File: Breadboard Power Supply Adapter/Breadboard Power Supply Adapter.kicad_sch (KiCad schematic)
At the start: 17 parts, among them J1 Conn_02x03_Odd_Even, J2 Conn_02x03_Odd_Even, J3 Conn_01x02, J4 Conn_01x02

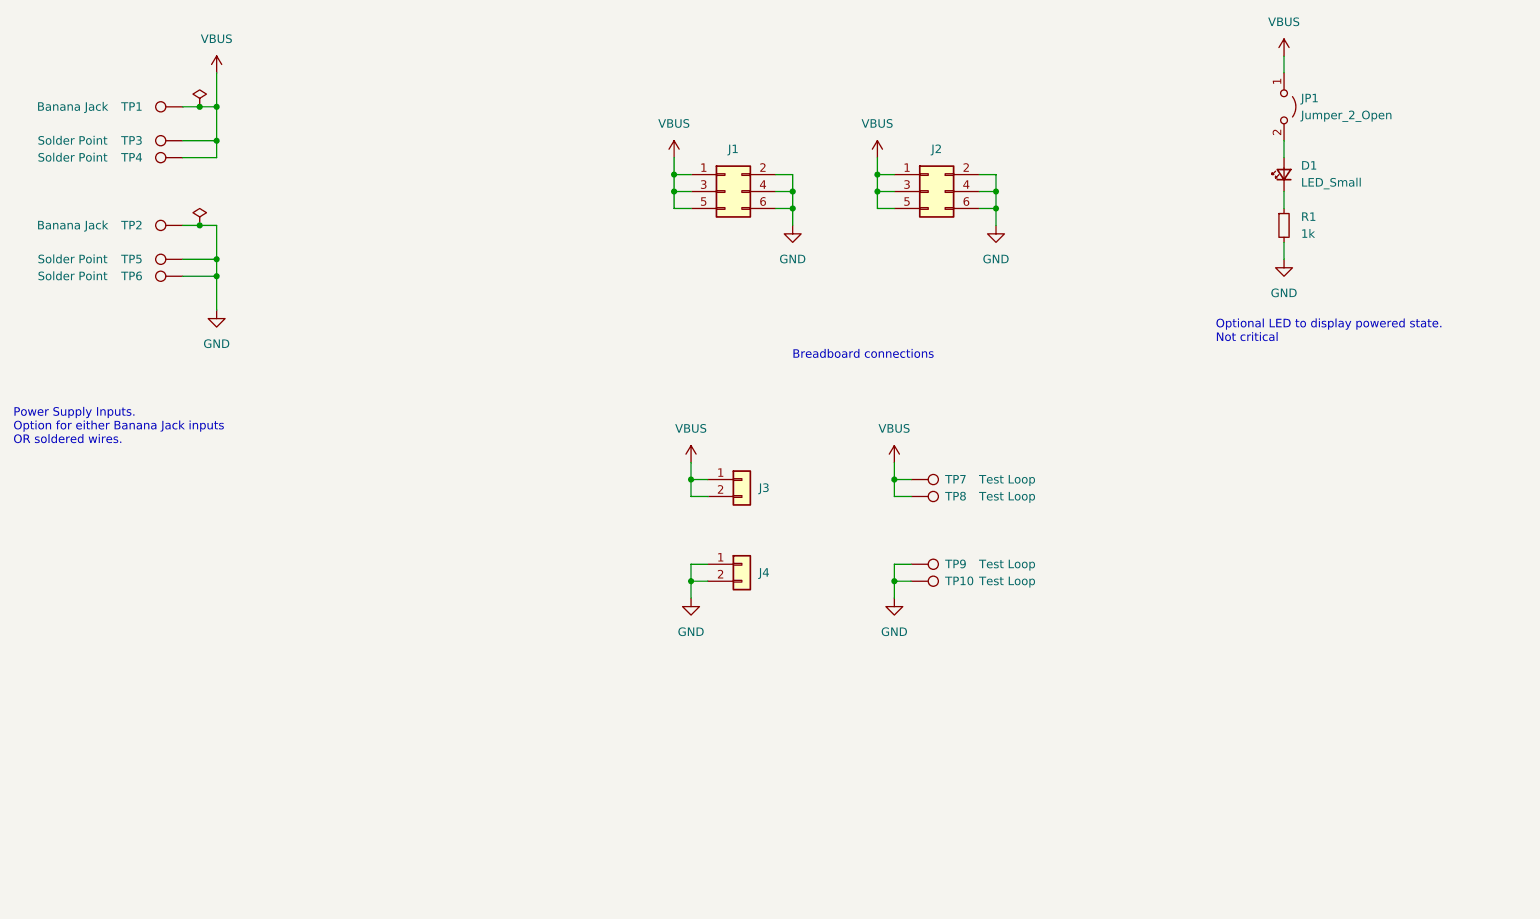
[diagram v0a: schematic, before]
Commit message: Made V2 Breadboard Power Supply Adapter
Removed several redundant test points.  Re-using the Banana jack pads is
sufficient for Keystone and wires.

Added 3-pin regulator footprint, along with output pin.  Could be used
for secondary voltage supply or reference regulator.
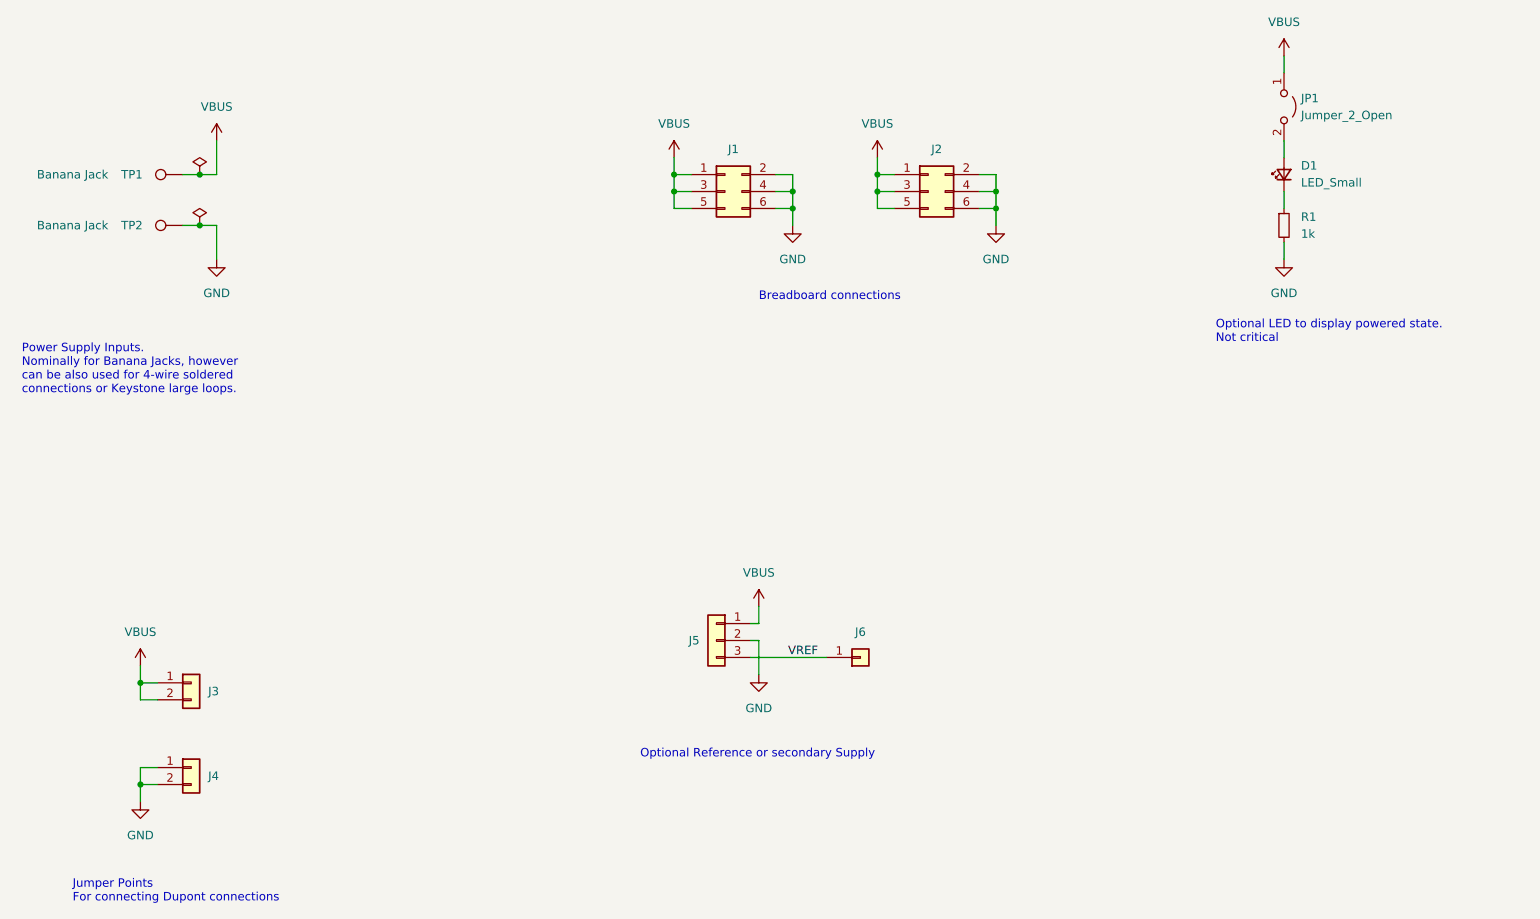
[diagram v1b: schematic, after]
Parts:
- removed TP10, TP7, TP8, TP9: Test Loop, TestPoint:TestPoint_Keystone_5010-5014_Multipurpose, symbol Connector:TestPoint
- removed TP3, TP5: Solder Point, Connector_Wire:SolderWire-2sqmm_1x01_D2mm_OD3.9mm, symbol Connector:TestPoint
- removed TP4, TP6: Solder Point, Connector_Wire:SolderWire-0.75sqmm_1x01_D1.25mm_OD3.5mm, symbol Connector:TestPoint
- added J5: Conn_01x03, Connector_PinHeader_2.54mm:PinHeader_1x03_P2.54mm_Vertical, symbol Connector_Generic:Conn_01x03
- added J6: Conn_01x01, TestPoint:TestPoint_Keystone_5010-5014_Multipurpose, symbol Connector_Generic:Conn_01x01
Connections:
- net GND: now also J5.2 (Pin_2)
- net VBUS: now also J5.1 (Pin_1)
- new net VREF: J5.3 (Pin_3), J6.1 (Pin_1)
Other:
- note added: "Jumper Points For connecting Dupont connections"
- note added: "Optional Reference or secondary Supply"
- note added: "Power Supply Inputs. Nominally for Banana Jacks, however can be also used for 4-wire soldered connections or Keystone large loops."
- note removed: "Power Supply Inputs. Option for either Banana Jack inputs OR soldered wires."
- company: (none) -> SK Electronics Consulting LLC
- title: (none) -> Breadboard Power Supply Adapter
- moved on the sheet: J3, J4, TP1
